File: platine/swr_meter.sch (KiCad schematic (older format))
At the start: 5 parts

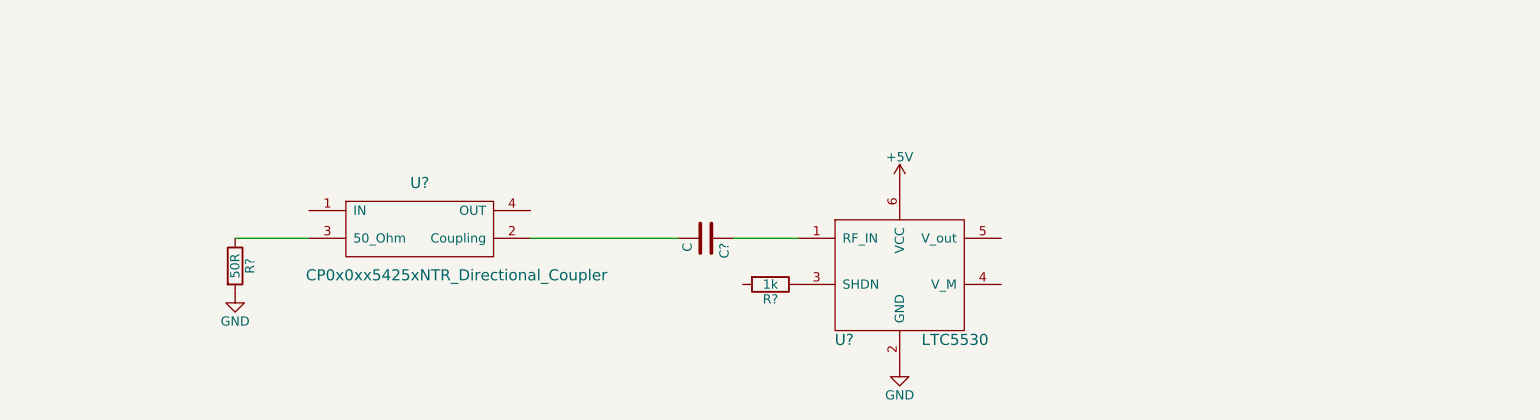
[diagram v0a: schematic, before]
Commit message: added new power detector
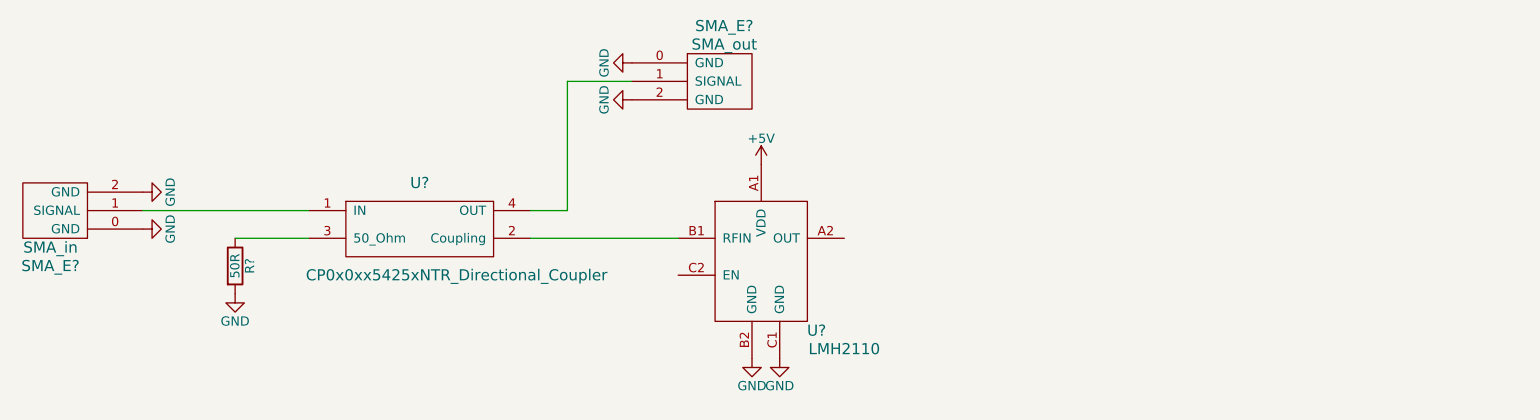
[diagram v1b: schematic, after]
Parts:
- removed C?: C, symbol C
- removed R?: 1k, symbol R
- removed U?: LTC5530, symbol LTC5530
- added SMA_E?: SMA_in, symbol SMA_EDGE
- added SMA_E?: SMA_out, symbol SMA_EDGE
- added U?: LMH2110, symbol LMH2110
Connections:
- net +5V: now also U?.A1 (VDD)
- net GND: now also SMA_E?.0 (GND), SMA_E?.0 (GND), SMA_E?.2 (GND), SMA_E?.2 (GND), U?.B2 (GND), U?.C1 (GND)
- net at U?.1 (IN): now also SMA_E?.1 (SIGNAL)
- net at U?.2 (Coupling): now also U?.B1 (RFIN)
- net at U?.4 (OUT): now also SMA_E?.1 (SIGNAL)
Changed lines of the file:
@@
 LIBS:cp0x0xx5425xntr_directional_coupler
 LIBS:ltc5530
+LIBS:toni
+LIBS:lmh2110
+LIBS:swr_meter-cache
 EELAYER 25 0
 EELAYER END
@@
 Wire Wire Line
 	2050 2200 2450 2200
+Wire Wire Line
+	3650 2200 4450 2200
 $Comp
-L LTC5530 U?
-U 1 1 570C0400
-P 5550 2200
-F 0 "U?" H 5350 1650 60  0000 C CNN
-F 1 "LTC5530" H 5950 1650 60  0000 C CNN
-F 2 "" H 5550 2200 60  0000 C CNN
-F 3 "" H 5550 2200 60  0000 C CNN
-	1    5550 2200
+L SMA_EDGE SMA_E?
+U 1 1 570D6441
+P 1200 2050
+F 0 "SMA_E?" H 1350 2350 60  0000 C CNN
+F 1 "SMA_in" H 1350 2250 60  0000 C CNN
+F 2 "" H 1200 2050 60  0000 C CNN
+F 3 "" H 1200 2050 60  0000 C CNN
+	1    1200 2050
+	-1   0    0    1
+$EndComp
+$Comp
+L SMA_EDGE SMA_E?
+U 1 1 570D66BE
+P 4550 1350
+F 0 "SMA_E?" H 4700 1650 60  0000 C CNN
+F 1 "SMA_out" H 4700 1550 60  0000 C CNN
+F 2 "" H 4550 1350 60  0000 C CNN
+F 3 "" H 4550 1350 60  0000 C CNN
+	1    4550 1350
 	1    0    0    -1
 $EndComp
+Wire Wire Line
+	2450 2050 1550 2050
 $Comp
-L R R?
-U 1 1 570C0526
-P 4950 2450
-F 0 "R?" V 5030 2450 50  0000 C CNN
-F 1 "1k" V 4950 2450 50  0000 C CNN
-F 2 "" V 4880 2450 50  0000 C CNN
-F 3 "" H 4950 2450 50  0000 C CNN
-	1    4950 2450
+L GND #PWR?
+U 1 1 570D67EB
+P 1550 1950
+F 0 "#PWR?" H 1550 1700 50  0001 C CNN
+F 1 "GND" H 1550 1800 50  0000 C CNN
+F 2 "" H 1550 1950 50  0000 C CNN
+F 3 "" H 1550 1950 50  0000 C CNN
+	1    1550 1950
+	0    -1   -1   0
+$EndComp
+$Comp
+L GND #PWR?
+U 1 1 570D6812
+P 1550 2150
+F 0 "#PWR?" H 1550 1900 50  0001 C CNN
+F 1 "GND" H 1550 2000 50  0000 C CNN
+F 2 "" H 1550 2150 50  0000 C CNN
+F 3 "" H 1550 2150 50  0000 C CNN
+	1    1550 2150
+	0    -1   -1   0
+$EndComp
+$Comp
+L GND #PWR?
+U 1 1 570D687A
+P 4200 1450
+F 0 "#PWR?" H 4200 1200 50  0001 C CNN
+F 1 "GND" H 4200 1300 50  0000 C CNN
+F 2 "" H 4200 1450 50  0000 C CNN
+F 3 "" H 4200 1450 50  0000 C CNN
+	1    4200 1450
 	0    1    1    0
 $EndComp
 $Comp
-L C C?
-U 1 1 570C0625
-P 4600 2200
-F 0 "C?" H 4625 2300 50  0000 L CNN
-F 1 "C" H 4625 2100 50  0000 L CNN
-F 2 "" H 4638 2050 50  0000 C CNN
-F 3 "" H 4600 2200 50  0000 C CNN
-	1    4600 2200
+L GND #PWR?
+U 1 1 570D689C
+P 4200 1250
+F 0 "#PWR?" H 4200 1000 50  0001 C CNN
+F 1 "GND" H 4200 1100 50  0000 C CNN
+F 2 "" H 4200 1250 50  0000 C CNN
+F 3 "" H 4200 1250 50  0000 C CNN
+	1    4200 1250
 	0    1    1    0
 $EndComp
 Wire Wire Line
-	4750 2200 5100 2200
+	3650 2050 3850 2050
 Wire Wire Line
-	3650 2200 4450 2200
+	3850 2050 3850 1350
+Wire Wire Line
+	3850 1350 4200 1350
 $Comp
-L +5V #PWR?
-U 1 1 570C068F
-P 5650 1900
-F 0 "#PWR?" H 5650 1750 50  0001 C CNN
-F 1 "+5V" H 5650 2040 50  0000 C CNN
-F 2 "" H 5650 1900 50  0000 C CNN
-F 3 "" H 5650 1900 50  0000 C CNN
-	1    5650 1900
+L LMH2110 U?
+U 1 1 570D7554
+P 4900 2300
+F 0 "U?" H 5200 1900 60  0000 C CNN
+F 1 "LMH2110" H 5350 1800 60  0000 C CNN
+F 2 "" H 4950 2300 60  0000 C CNN
+F 3 "" H 4950 2300 60  0000 C CNN
+	1    4900 2300
 	1    0    0    -1
 $EndComp
 $Comp
 L GND #PWR?
-U 1 1 570C06AD
-P 5650 2900
-F 0 "#PWR?" H 5650 2650 50  0001 C CNN
-F 1 "GND" H 5650 2750 50  0000 C CNN
-F 2 "" H 5650 2900 50  0000 C CNN
-F 3 "" H 5650 2900 50  0000 C CNN
-	1    5650 2900
+U 1 1 570D75A8
+P 4850 2850
+F 0 "#PWR?" H 4850 2600 50  0001 C CNN
+F 1 "GND" H 4850 2700 50  0000 C CNN
+F 2 "" H 4850 2850 50  0000 C CNN
+F 3 "" H 4850 2850 50  0000 C CNN
+	1    4850 2850
 	1    0    0    -1
 $EndComp
+$Comp
+L GND #PWR?
+U 1 1 570D75C9
+P 5000 2850
+F 0 "#PWR?" H 5000 2600 50  0001 C CNN
+F 1 "GND" H 5000 2700 50  0000 C CNN
+F 2 "" H 5000 2850 50  0000 C CNN
+F 3 "" H 5000 2850 50  0000 C CNN
+	1    5000 2850
+	1    0    0    -1
+$EndComp
+$Comp
+L +5V #PWR?
+U 1 1 570D7623
+P 4900 1800
+F 0 "#PWR?" H 4900 1650 50  0001 C CNN
+F 1 "+5V" H 4900 1940 50  0000 C CNN
+F 2 "" H 4900 1800 50  0000 C CNN
+F 3 "" H 4900 1800 50  0000 C CNN
+	1    4900 1800
+	1    0    0    -1
+$EndComp

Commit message: changed back to lt power detector because of bad input impedance of the ti power detector (page 10 figure 7 of LMH2110 datasheet)
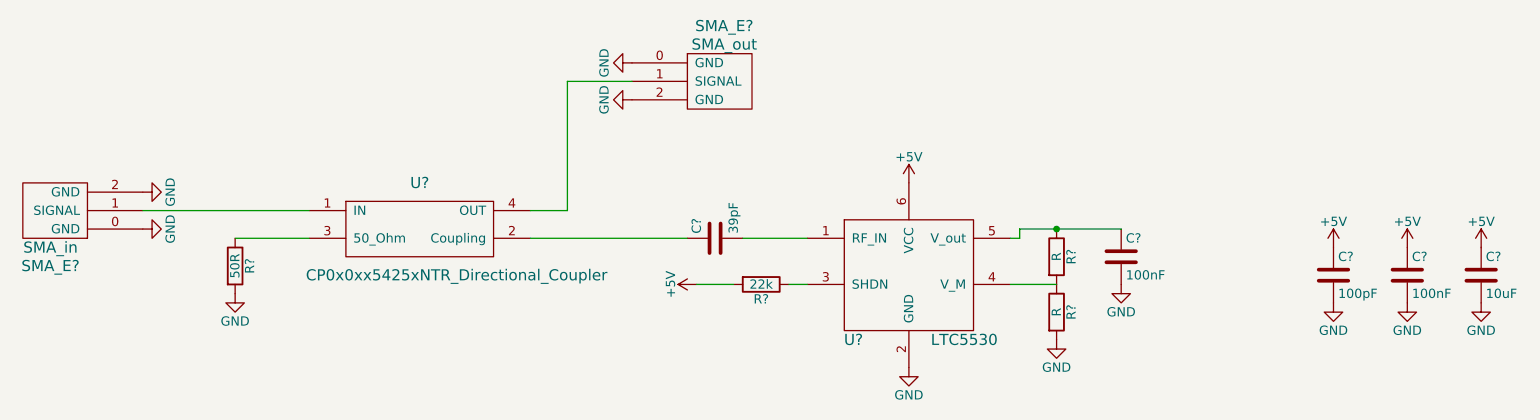
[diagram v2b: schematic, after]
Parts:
- removed U?: LMH2110, symbol LMH2110
- added C? (x2): 100nF, symbol C
- added C?: 10uF, symbol C
- added C?: 100pF, symbol C
- added C?: 39pF, symbol C
- added R?: 22k, symbol R
- added R? (x2): R, symbol R
- added U?: LTC5530, symbol LTC5530
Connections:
- net +5V: now also C?.1, C?.1, C?.1, R?.2, U?.6 (VCC)
- net GND: now also C?.2, C?.2, C?.2, C?.2, R?.2, U?.2 (GND)
- net at U?.2 (Coupling): now also C?.1
- new net: C?.2, U?.1 (RF_IN)
- new net: R?.1, U?.3 (SHDN)
- new net: R?.1, R?.2, U?.4 (V_M)
- new net: C?.1, R?.1, U?.5 (V_out)
